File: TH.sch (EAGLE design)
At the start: 52 parts, among them IC1 TLE5205-2G, IC2 TLE5205-2G, IC3 TLE5205-2G, IC5 TLE5205-2G, J3 POWERPOLE_DOUBLE, M0 Motor3, M1 Motor3, M2 Motor3, M3 Motor3, U1 LM2576.SMD

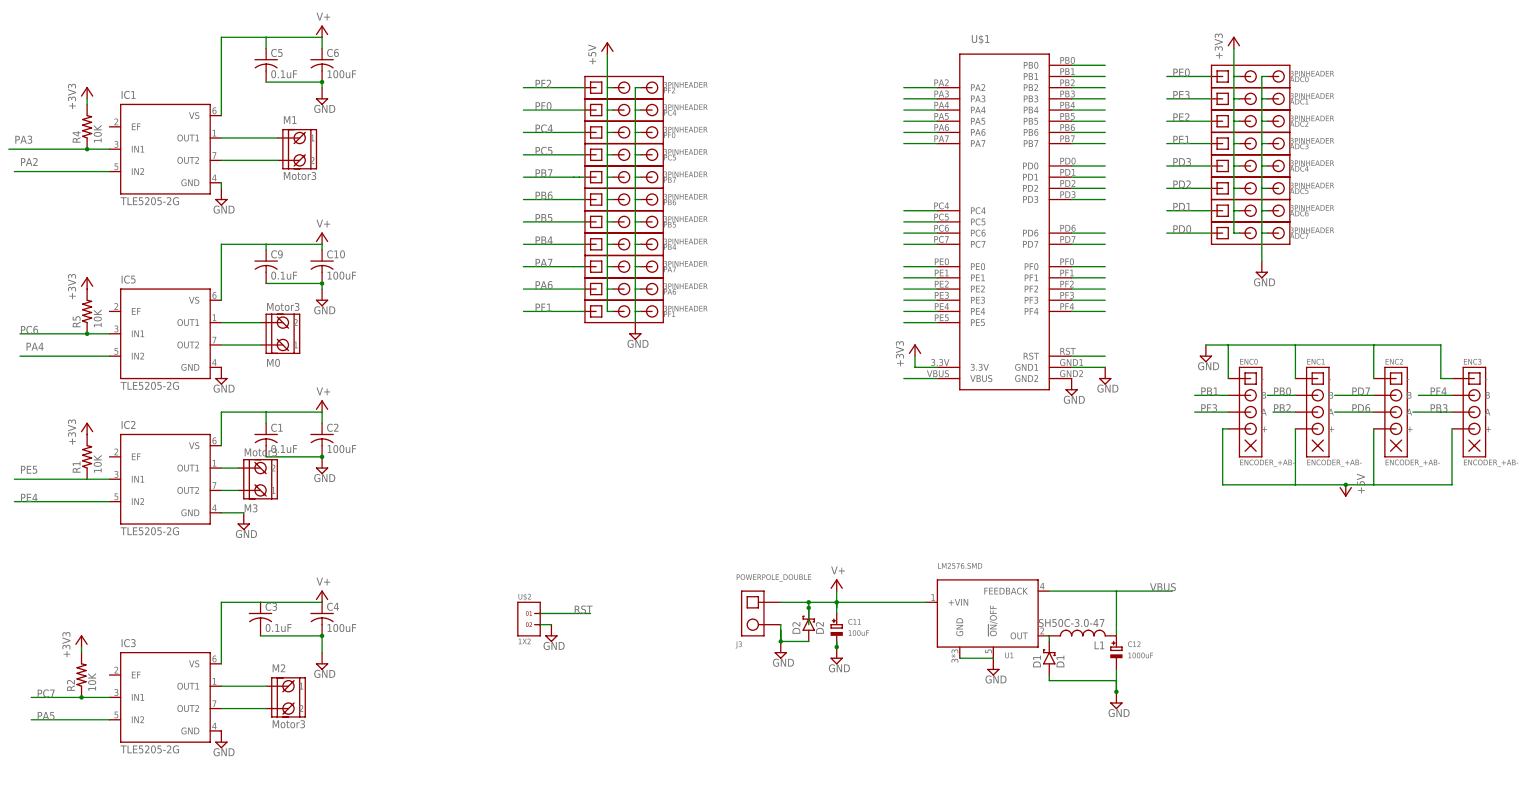
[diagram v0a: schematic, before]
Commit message: Made new file for Through hole
Changed all components to through hole expect power regulator because
eagle won't let me make a bigger board in the free version
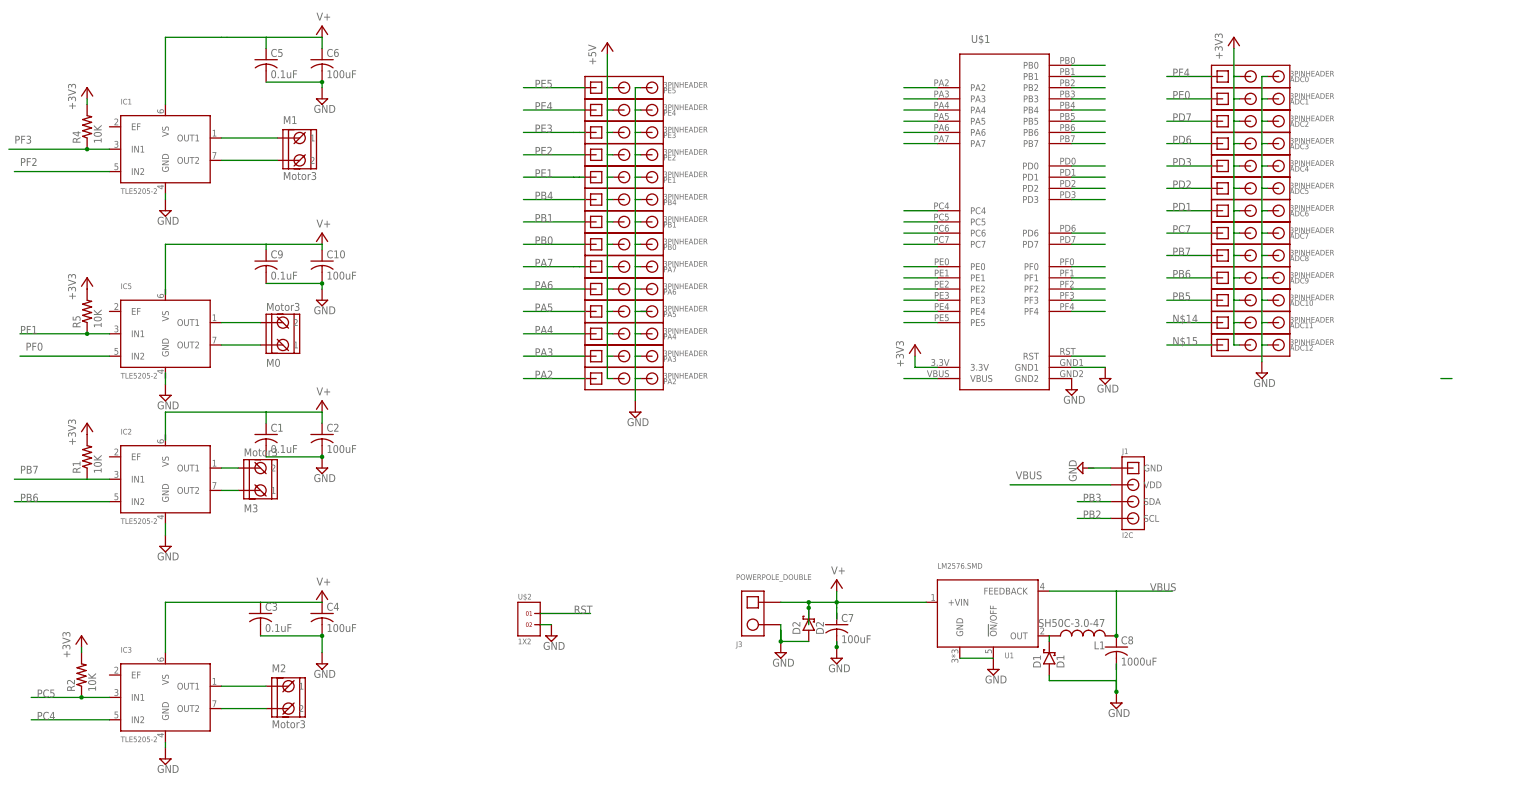
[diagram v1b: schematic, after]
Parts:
- removed C11: 100uF, microbuilder:CAP_ELECTROLYTICPANASONIC_D
- removed C12: 1000uF, microbuilder:CAP_ELECTROLYTICPANASONIC_D
- removed ENC0, ENC1, ENC2, ENC3: ENCODER_+AB-, RASEagleLib:ENCODER_+AB-
- removed PB6: 3PINHEADER, RASEagleLib:3PINHEADER
- added ADC10, ADC11, ADC12, ADC8, ADC9, PA2, PA3, PA4, PB0: 3PINHEADER, RASEagleLib:3PINHEADER
- added C7: 100uF, resistor:C-US025-050X050
- added C8: 1000uF, resistor:C-US025-050X050
- added J1: I2C, RASEagleLib:I2C
- C1, C10, C2, C3, C4, C5, C6, C9: device resistor:C-USC0603 -> resistor:C-US025-024X044
- IC1, IC2, IC3, IC5: value TLE5205-2G -> TLE5205-2; device infineon:TLE5205-2G -> RASEagleLib:TLE5205-2
- R1, R2, R4, R5: device resistor:R-US_R0603 -> resistor:R-US_0204/7
- renumbered PB5 to PB1, PB7 to PE1, PC4 to PE4, PC5 to PE2, PF0 to PE3, PF1 to PA5, PF2 to PE5
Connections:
- removed net +5V: ENC0.+, ENC1.+, ENC2.+, ENC3.+, PA5.2, PA6.2, PA7.2, PB1.2, PB4.2, PB6.2, PE1.2, PE2.2, PE3.2, PE4.2, PE5.2
- new net GND: IC1.GND, IC2.GND, IC3.GND
- new net N$10: J1.GND
- new net N$14: ADC11.1
- new net N$15: ADC12.1
- net +3V3: now also ADC10.2, ADC11.2, ADC12.2, ADC8.2, ADC9.2
- net -GND: now also ADC10.3, ADC11.3, ADC12.3, ADC8.3, ADC9.3, C7.2, C8.2, PA2.3, PA3.3, PA4.3, PB0.3; no longer C11.-, C12.-, ENC0.-, ENC1.-, ENC2.-, ENC3.-, IC1.GND, IC2.GND, IC3.GND, IC5.GND, PB6.3
- net PA2: now also PA2.1; no longer IC1.IN2
- net PA3: now also PA3.1; no longer IC1.IN1, R4.1
- net PA4: now also PA4.1; no longer IC5.IN2
- net PA5: now also PA5.1; no longer IC3.IN2
- net PB0: now also PB0.1; no longer ENC1.B
- net PB1: now also PB1.1; no longer ENC0.B
- net PB2: now also J1.SCL; no longer ENC1.A
- net PB3: now also J1.SDA; no longer ENC3.A
- net PB5: now also ADC10.1; no longer PB1.1
- net PB6: now also ADC9.1, IC2.IN2; no longer PB6.1
- net PB7: now also ADC8.1, IC2.IN1, R1.1; no longer PE1.1
- net PC4: now also IC3.IN2; no longer PE3.1
- net PC5: now also IC3.IN1, R2.1; no longer PE2.1
- net PC6: no longer IC5.IN1, R5.1
- net PC7: now also ADC7.1; no longer IC3.IN1, R2.1
- net PD0: no longer ADC7.1
- net PD6: now also ADC3.1; no longer ENC2.A
- net PD7: now also ADC2.1; no longer ENC2.B
- net PE0: now also ADC1.1; no longer ADC0.1
- net PE1: now also PE1.1; no longer ADC3.1
- net PE2: now also PE2.1; no longer ADC2.1
- net PE3: now also PE3.1; no longer ADC1.1
- net PE4: now also PE4.1; no longer IC2.IN2
- net PE5: now also PE5.1; no longer IC2.IN1, R1.1
- net PF0: now also IC5.IN2; no longer PE4.1
- net PF1: now also IC5.IN1, R5.1; no longer PA5.1
- net PF2: now also IC1.IN2; no longer PE5.1
- net PF3: now also IC1.IN1, R4.1; no longer ENC0.A
- net PF4: now also ADC0.1; no longer ENC3.B
- net V+: now also C7.1; no longer C11.+, IC2.VS, IC5.VS
- net VBUS: now also C8.1, J1.VDD, PA2.2, PA3.2, PA4.2, PA5.2, PA6.2, PA7.2, PB0.2, PB1.2, PB4.2, PE1.2, PE2.2, PE3.2, PE4.2, PE5.2; no longer C12.+
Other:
- moved on the sheet: PB4

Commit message: Finished Traces
Only thing left to do is label everything, and ground layer, with do
this tomorrow after TRR
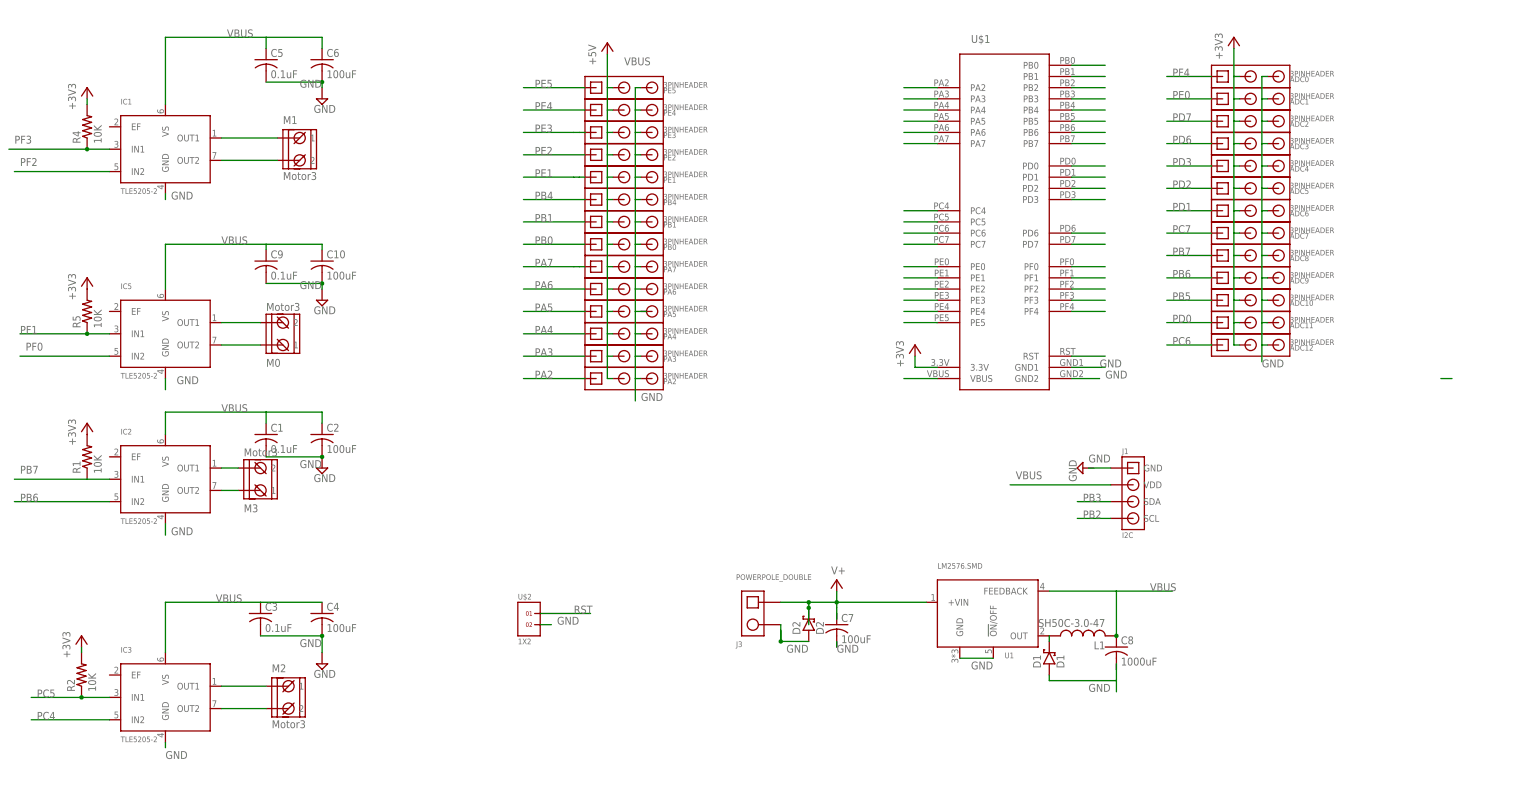
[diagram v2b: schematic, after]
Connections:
- removed net -GND: ADC0.3, ADC1.3, ADC10.3, ADC11.3, ADC12.3, ADC2.3, ADC3.3, ADC4.3, ADC5.3, ADC6.3, ADC7.3, ADC8.3, ADC9.3, C1.2, C10.2, C2.2, C3.2, C4.2, C5.2, C6.2, C7.2, C8.2, C9.2, D1.A, D2.A, J3.2, PA2.3, PA3.3, PA4.3, PA5.3, PA6.3, PA7.3, PB0.3, PB1.3, PB4.3, PE1.3, PE2.3, PE3.3, PE4.3, PE5.3, U$1.GND1, U$1.GND2, U$2.2, U1.!ON!/OFF, U1.GND
- removed net N$10: J1.GND
- removed net N$14: ADC11.1
- removed net N$15: ADC12.1
- net GND: now also ADC0.3, ADC1.3, ADC10.3, ADC11.3, ADC12.3, ADC2.3, ADC3.3, ADC4.3, ADC5.3, ADC6.3, ADC7.3, ADC8.3, ADC9.3, C1.2, C10.2, C2.2, C3.2, C4.2, C5.2, C6.2, C7.2, C8.2, C9.2, D1.A, D2.A, IC5.GND, J1.GND, J3.2, PA2.3, PA3.3, PA4.3, PA5.3, PA6.3, PA7.3, PB0.3, PB1.3, PB4.3, PE1.3, PE2.3, PE3.3, PE4.3, PE5.3, U$1.GND1, U$1.GND2, U$2.2, U1.!ON!/OFF, U1.GND
- net PC6: now also ADC12.1
- net PD0: now also ADC11.1
- net V+: no longer C1.1, C10.1, C2.1, C3.1, C4.1, C5.1, C6.1, C9.1, IC1.VS, IC3.VS
- net VBUS: now also C1.1, C10.1, C2.1, C3.1, C4.1, C5.1, C6.1, C9.1, IC1.VS, IC2.VS, IC3.VS, IC5.VS

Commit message: Final Design
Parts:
- removed ADC11, ADC12: 3PINHEADER, RASEagleLib:3PINHEADER
- added D3: D2, RASEagleLib:1N5820-D
- added R3, R6: 10K, resistor:R-US_0204/7
- PB7: value Motor3 -> PB6
- PC4: value Motor3 -> PC5
- PF1: value Motor3 -> PF0
- PF2: value Motor3 -> PF3
- renumbered ADC0 to PF4, ADC1 to PE0, ADC10 to PC6, ADC2 to PD7, ADC3 to PD6, ADC4 to PD3, ADC5 to PD2, ADC6 to PD1, ADC7 to PC7, ADC8 to PB5, ADC9 to PD0, M0 to PF1, M1 to PF2, M2 to PC4, M3 to PB7
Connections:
- removed net +3V3: ADC11.2, ADC12.2, PB5.2, PC6.2, PC7.2, PD0.2, PD1.2, PD2.2, PD3.2, PD6.2, PD7.2, PE0.2, PF4.2, R1.2, R2.2, R4.2, R5.2, U$1.3.3V
- new net 3.3V: J1.VDD, PA2.2, PB5.2, PC6.2, PC7.2, PD0.2, PD1.2, PD2.2, PD3.2, PD6.2, PD7.2, PE0.2, PF4.2, R3.2, R6.2, U$1.3.3V
- new net N$5$: C8.1, D3.A, L1.2, U1.FEEDBACK
- net GND: now also R1.2, R2.2, R4.2, R5.2; no longer ADC11.3, ADC12.3, PA2.3
- net PB2: now also R6.1
- net PB3: now also R3.1
- net PB5: now also PB5.1; no longer PC6.1
- net PB6: no longer PD0.1
- net PB7: no longer PB5.1
- net PC6: now also PC6.1; no longer ADC12.1
- net PD0: now also PD0.1; no longer ADC11.1
- net V+: now also C1.1, C10.1, C2.1, C3.1, C4.1, C5.1, C6.1, C9.1, IC1.VS, IC2.VS, IC3.VS, IC5.VS
- net VBUS: now also D3.C; no longer C1.1, C10.1, C2.1, C3.1, C4.1, C5.1, C6.1, C8.1, C9.1, IC1.VS, IC2.VS, IC3.VS, IC5.VS, J1.VDD, L1.2, PA2.2, U1.FEEDBACK
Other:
- moved on the sheet: PA2
